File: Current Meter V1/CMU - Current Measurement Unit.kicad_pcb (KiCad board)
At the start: 4 copper layers, 55.3 x 79.8 mm, 36 parts, among them J401 I2C OLED Display Connector, J501 Connector, U201 MCP6002-xSN, U601 TPS5430DDAR

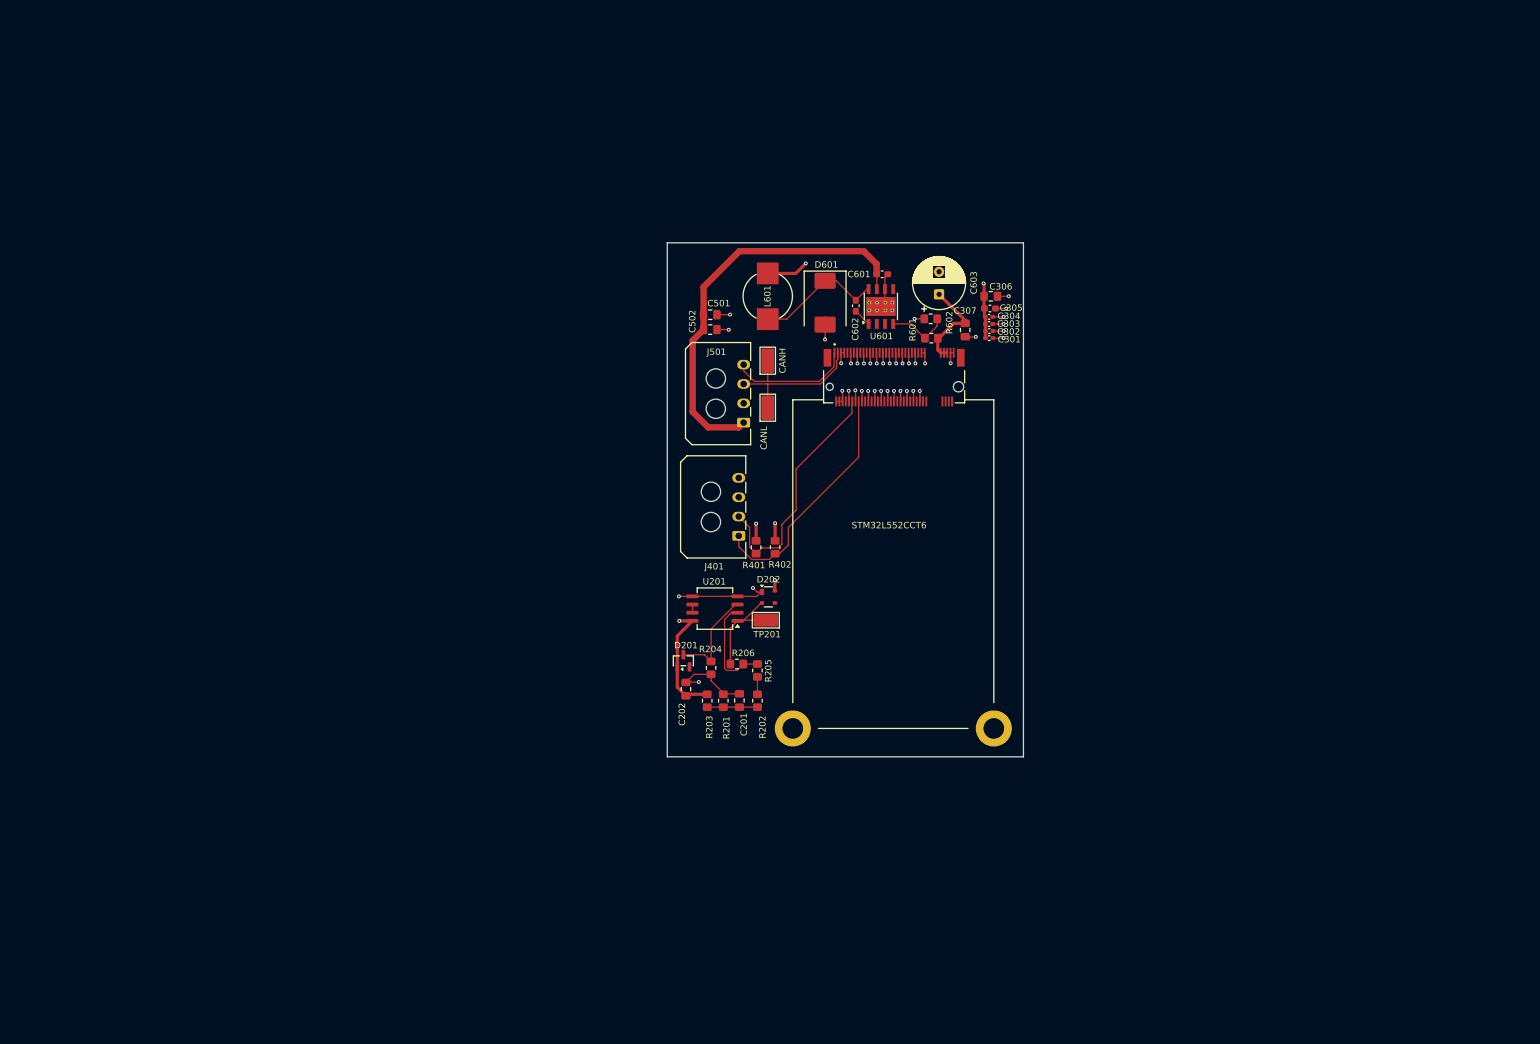
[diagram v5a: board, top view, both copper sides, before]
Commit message: added sensor connector, updated pcb layout
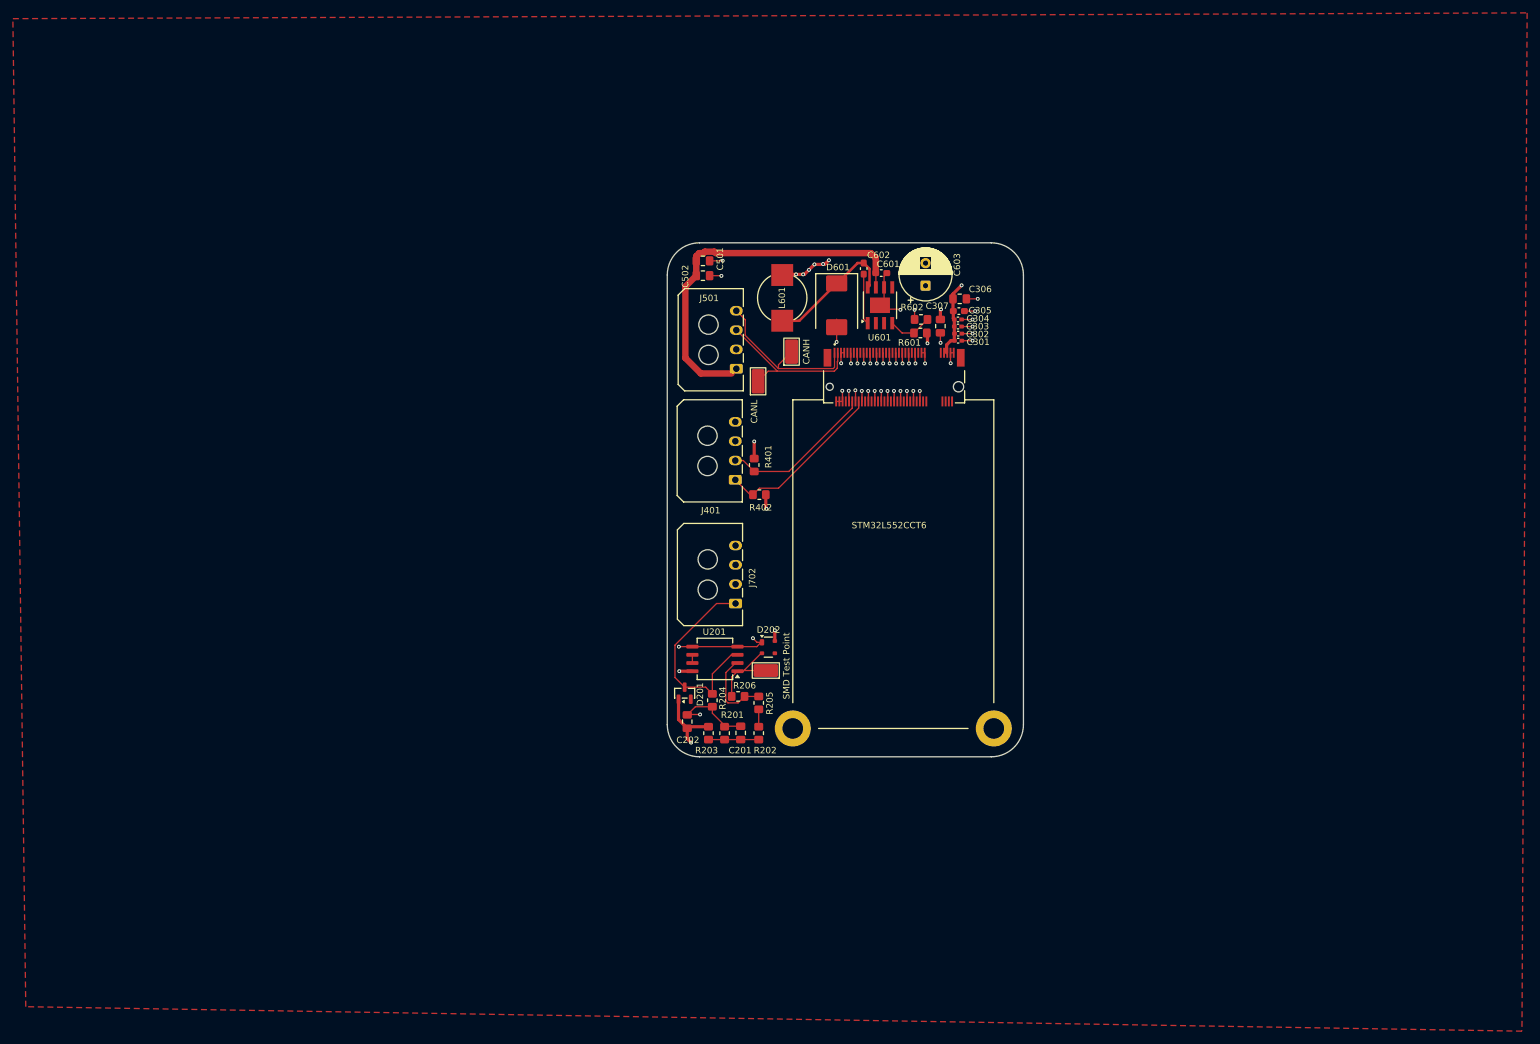
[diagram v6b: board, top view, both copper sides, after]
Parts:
- added G***: LOGO, images:gudetama, B.Cu at (165.1, 124.7)
- added G***: LOGO, bfr_logos:BFR_Small, B.Cu at (161.5, 132.1)
- added J702: Sensor Connector, Connector_Molex:Molex_Micro-Fit_3.0_43650-0400_1x04_P3.00mm_Horizontal, F.Cu at (135.6, 121.0)
- TP201: footprint TestPoint:TestPoint_Keystone_5019_Miniature -> bfr_utilities:TestPoint_Keystone_5019_Miniature
- U601: footprint Package_SO:TI_SO-PowerPAD-8_ThermalVias -> Package_SO:TI_SO-PowerPAD-8
- moved R401 12.8 mm to (138.5, 99.5)
- moved J401 8.72 mm to (135.6, 101.8)
- moved R402 8.52 mm to (139.3, 104.1), turned to 0 degrees
- moved C501 8.44 mm to (130.5, 67.8)
- moved C502 8.44 mm to (130.5, 70.1)
- moved J501 8.44 mm to (135.7, 84.5)
- moved D202 7.81 mm to (140.7, 127.8)
- moved TP201 7.81 mm to (140.3, 131.4)
- moved U201 7.81 mm to (132.4, 129.6)
- moved C602 5.91 mm to (155.5, 69.0)
- moved C202 5.04 mm to (128.1, 139.3)
- moved C201 5.04 mm to (136.4, 141.1)
- moved R201 5.04 mm to (133.9, 141.1)
- moved R203 5.04 mm to (131.4, 141.1)
- moved D201 5.04 mm to (127.7, 134.9)
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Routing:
- net /opamp/2.5V, 0.55V-4.5V: track 15.5 -> 32.2 mm
- net /display/I2C_SCL: track 38.2 -> 24.0 mm
- net +5_V: track 55.6 -> 43.8 mm, vias 6 -> 14
- net /display/I2C_SDA: track 37.9 -> 26.7 mm
- net /buck/+12_V: track 63.4 -> 57.9 mm
- net Net-(U601-BOOT): track 2.79 -> 7.89 mm
- net /connector/CAN+: track 22.0 -> 26.2 mm
- net Net-(U201A--): track 15.7 -> 12.5 mm
- net /connector/CAN-: track 21.6 -> 24.6 mm
- net Net-(U601-VSENSE): track 9.85 -> 6.97 mm
- net /opamp/Gain=0.833, 1.67 (0-3.3): track 16.5 -> 13.6 mm
- net GND: track 99.7 -> 102.1 mm, vias 41 -> 42
- net /buck/SW_NODE: track 20.1 -> 20.6 mm
- added copper zone on F.Cu, net +5_V
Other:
- outline, holes or cut-outs redrawn

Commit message: updated layout, added sensor connector
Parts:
- moved G*** 4.13 mm to (163.7, 120.8)

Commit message: basically done board layout (hopefully)
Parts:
- moved R401 2.60 mm to (141.1, 99.5)
- moved TP302 2.33 mm to (140.8, 88.1)
- moved R402 1.30 mm to (140.6, 104.1)
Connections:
- J702 pad 2: GND -> /sensorConnector/V_REF
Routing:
- net /display/I2C_SDA: track 26.7 -> 32.5 mm
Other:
- board text added: "12V_IN GND CAN- CAN+"
- board text added: "CAN Connector"
- board text added: "Display Connector"
- board text added: "SDA SCL 5V_IN GND"
- board text added: "Sensor Connector"
- board text added: "V_OUT V_REF GND 5V_IN"
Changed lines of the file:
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@@
 	(net 48 "unconnected-(U601-NC-Pad2)")
 	(net 49 "unconnected-(U601-EN-Pad5)")
+	(net 50 "/sensorConnector/V_REF")
 	(footprint "Resistor_SMD:R_0805_2012Metric_Pad1.20x1.40mm_HandSolder"
 		(layer "F.Cu")
@@
 	(footprint "Resistor_SMD:R_0805_2012Metric_Pad1.20x1.40mm_HandSolder"
 		(layer "F.Cu")
-		(at 138.5 99.5 90)
+		(at 141.1 99.53 90)
 		(descr "Resistor SMD 0805 (2012 Metric), square (rectangular) end terminal, IPC-7351 nominal with elongated pad for handsoldering. (Body size source: IPC-SM-782 page 72, https://www.pcb-3d.com/wordpress/wp-content/uploads/ipc-sm-782a_amendment_1_and_2.pdf), generated with kicad-footprint-generator")
 		(tags "resistor handsolder")
@@
 		(tags "connector Molex Micro-Fit_3.0 horizontal")
 		(property "Reference" "J702"
-			(at 4 2.6 90)
+			(at 3.7 5.1 90)
 			(layer "F.SilkS")
 			(effects
@@
 		)
 		(property "Value" "Sensor Connector"
-			(at 4.5 3.22 90)
+			(at 4.5 5 90)
 			(layer "F.Fab")
 			(effects
@@
 			(layers "*.Cu" "*.Mask")
 			(remove_unused_layers no)
-			(net 1 "GND")
-			(pinfunction "2")
+			(net 50 "/sensorConnector/V_REF")
+			(pinfunction "V_REF")
 			(pintype "passive")
 		)
@@
 	(footprint "bfr_utilities:TestPoint_Keystone_5019_Miniature"
 		(layer "F.Cu")
-		(at 139.1 86.5 90)
+		(at 140.8 88.1 90)
 		(descr "Keystone SMT Miniature Test Point 5019, http://www.keyelco.com/product-pdf.cfm?p=1357")
 		(tags "Test Point")
@@
 		)
 		(property "Value" "CANL"
-			(at -4.7 -0.6 90)
+			(at -4.3 0.8 90)
 			(layer "F.SilkS")
 			(effects
@@
 	(footprint "Resistor_SMD:R_0805_2012Metric_Pad1.20x1.40mm_HandSolder"
 		(layer "F.Cu")
-		(at 139.3 104.1)
+		(at 140.6 104.1)
 		(descr "Resistor SMD 0805 (2012 Metric), square (rectangular) end terminal, IPC-7351 nominal with elongated pad for handsoldering. (Body size source: IPC-SM-782 page 72, https://www.pcb-3d.com/wordpress/wp-content/uploads/ipc-sm-782a_amendment_1_and_2.pdf), generated with kicad-footprint-generator")
 		(tags "resistor handsolder")
@@
 		(layer "Edge.Cuts")
 	)
+	(gr_text "Display Connector\n"
+		(at 129 103.6 90)
+		(layer "F.SilkS")
+		(effects
+			(font
+				(size 1 1)
+				(thickness 0.1)
+			)
+			(justify left bottom)
+		)
+	)
+	(gr_text "CAN Connector\n"
+		(at 129.1 86.1 90)
+		(layer "F.SilkS")
+		(effects
+			(font
+				(size 1 1)
+				(thickness 0.1)
+			)
+			(justify left bottom)
+		)
+	)
+	(gr_text "SDA SCL 5V_IN GND\n"
+		(at 138.4 104.835 90)
+		(layer "F.SilkS")
+		(effects
+			(font
+				(size 0.889 0.889)
+				(thickness 0.1)
+			)
+			(justify left bottom)
+		)
+	)
+	(gr_text "V_OUT V_REF GND 5V_IN"
+		(at 138.5 124.8 90)
+		(layer "F.SilkS")
+		(effects
+			(font
+				(size 0.889 0.889)
+				(thickness 0.1)
+			)
+			(justify left bottom)
+		)
+	)
+	(gr_text "Sensor Connector\n"
+		(at 128.9 122.8 90)
+		(layer "F.SilkS")
+		(effects
+			(font
+				(size 1 1)
+				(thickness 0.1)
+			)
+			(justify left bottom)
+		)
+	)
+	(gr_text "12V_IN GND CAN- CAN+"
+		(at 138.4 87.1 90)
+		(layer "F.SilkS")
+		(effects
+			(font
+				(size 0.889 0.762)
+				(thickness 0.1)
+			)
+			(justify left bottom)
+		)
+	)
 	(segment
 		(start 155.5 82.105)
@@
 	)
 	(segment
-		(start 140.3 106.2)
-		(end 140.4 106.3)
+		(start 141.6 106.2)
+		(end 141.7 106.3)
 		(width 0.5)
 		(layer "F.Cu")
@@
 	)
 	(segment
-		(start 140.3 104.1)
-		(end 140.3 106.2)
+		(start 141.6 104.1)
+		(end 141.6 106.2)
 		(width 0.5)
 		(layer "F.Cu")
@@
 	)
 	(segment
-		(start 138.5 95.84)
-		(end 138.5 98.5)
+		(start 141.1 95.87)
+		(end 141.1 98.53)
 		(width 0.5)
 		(layer "F.Cu")
@@
 	)
 	(via
-		(at 140.4 106.3)
+		(at 141.7 106.3)
 		(size 0.6)
 		(drill 0.3)
@@
 	)
 	(via
-		(at 138.5 95.84)
+		(at 141.1 95.87)
 		(size 0.6)
 		(drill 0.3)
@@
 	)
 	(segment
-		(start 137.865 104.1)
-		(end 138.3 104.1)
-		(width 0.2)
+		(start 137.3 101.8)
+		(end 139.6 104.1)
+		(width 0.3)
 		(layer "F.Cu")
 		(net 8)
 	)
 	(segment
-		(start 154.72 90.652)
-		(end 154.72 89.625)
+		(start 152.201 103.099)
+		(end 140.601 103.099)
 		(width 0.2)
 		(layer "F.Cu")
@@
 	)
 	(segment
-		(start 142.272 103.1)
-		(end 154.72 90.652)
-		(width 0.2)
+		(start 135.565 101.8)
+		(end 137.3 101.8)
+		(width 0.3)
 		(layer "F.Cu")
 		(net 8)
 	)
 	(segment
-		(start 135.565 101.8)
-		(end 137.865 104.1)
+		(start 154.72 89.625)
+		(end 154.72 100.58)
 		(width 0.2)
 		(layer "F.Cu")
@@
 	)
 	(segment
-		(start 139.3 103.1)
-		(end 142.272 103.1)
+		(start 154.72 100.58)
+		(end 152.201 103.099)
 		(width 0.2)
 		(layer "F.Cu")
@@
 	)
 	(segment
-		(start 138.3 104.1)
-		(end 139.3 103.1)
+		(start 140.601 103.099)
+		(end 139.6 104.1)
 		(width 0.2)
 		(layer "F.Cu")
@@
 	)
 	(segment
-		(start 153.72 90.652)
-		(end 153.72 89.625)
+		(start 143.842 100.53)
+		(end 153.72 90.652)
 		(width 0.2)
 		(layer "F.Cu")
@@
 	)
 	(segment
-		(start 143.872 100.5)
-		(end 153.72 90.652)
+		(start 141.1 100.53)
+		(end 143.842 100.53)
 		(width 0.2)
 		(layer "F.Cu")
@@
 	)
 	(segment
-		(start 138.5 100.5)
-		(end 143.872 100.5)
+		(start 139.37 98.8)
+		(end 141.1 100.53)
 		(width 0.2)
 		(layer "F.Cu")
@@
 	)
 	(segment
-		(start 135.565 98.8)
-		(end 136.8 98.8)
+		(start 153.72 90.652)
+		(end 153.72 89.625)
 		(width 0.2)
 		(layer "F.Cu")
@@
 	)
 	(segment
-		(start 136.8 98.8)
-		(end 138.5 100.5)
+		(start 135.565 98.8)
+		(end 139.37 98.8)
 		(width 0.2)
 		(layer "F.Cu")
@@
 	)
 	(segment
-		(start 140.673 84.927)
-		(end 142.097 84.927)
+		(start 140.8 88.1)
+		(end 142.097 86.803)
 		(width 0.2)
 		(layer "F.Cu")
@@
 	)
 	(segment
-		(start 135.72 78.55)
+		(start 142.097 86.803)
 		(end 142.097 84.927)
 		(width 0.2)
@@
 	)
 	(segment
-		(start 139.1 86.5)
-		(end 140.673 84.927)
+		(start 135.72 78.55)
+		(end 142.097 84.927)
 		(width 0.2)
 		(layer "F.Cu")
